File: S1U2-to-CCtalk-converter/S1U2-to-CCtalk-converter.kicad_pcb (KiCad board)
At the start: 2 copper layers, 136.2 x 73.1 mm, 23 parts, among them J1 DB9_Female, J2 CCtalk Cable, J3 CCtalk Cable, Q1 BC847, Q2 BC856, U1 ST232B, U2 L7805

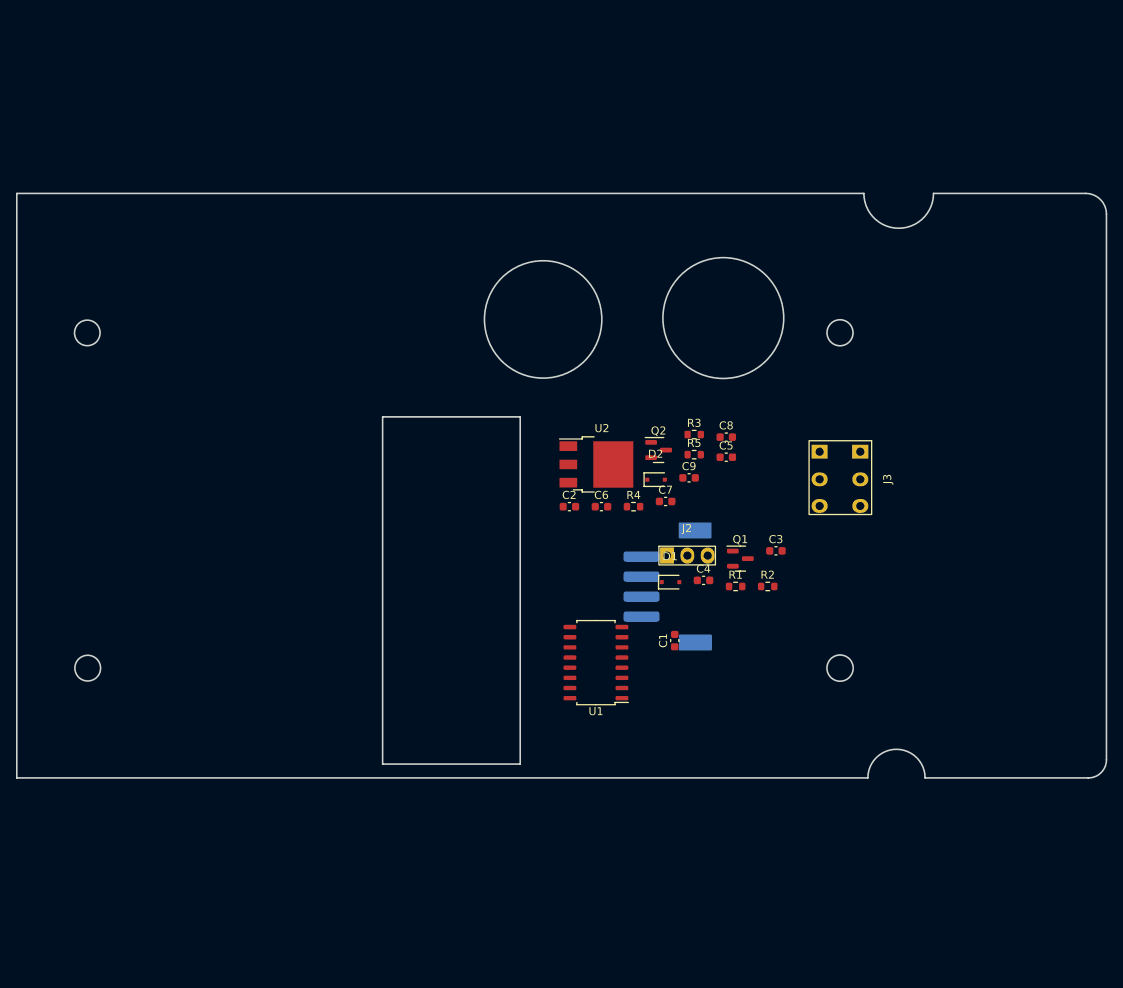
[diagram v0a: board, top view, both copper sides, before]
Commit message: add s1u2 dxf bckg and place components
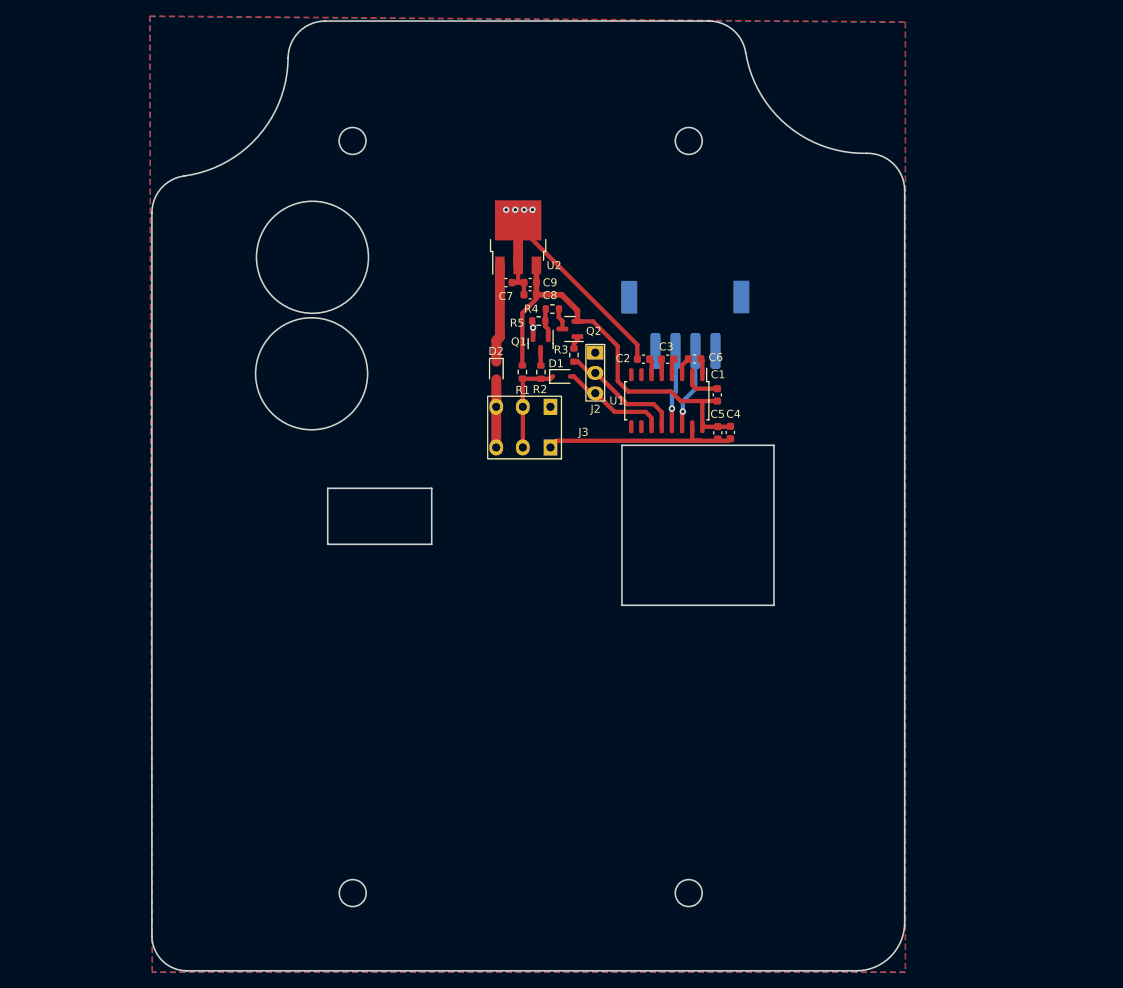
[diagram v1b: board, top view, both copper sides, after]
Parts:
- moved J3 39.7 mm to (140.3, 90.4), turned to 180 degrees
- moved R2 39.0 mm to (140.0, 80.9), turned to -90 degrees
- moved R1 37.8 mm to (137.7, 80.9), turned to -90 degrees
- moved Q1 36.7 mm to (140.0, 77.4), turned to -90 degrees
- moved J1 34.5 mm to (161.8, 78.3), turned to 180 degrees
- moved U1 33.9 mm to (155.7, 84.5), turned to -90 degrees
- moved C7 33.9 mm to (135.6, 69.8)
- moved C9 31.5 mm to (138.7, 69.8), turned to 180 degrees
- moved C1 31.2 mm to (162.0, 83.8)
- moved U2 30.9 mm to (137.2, 63.4), turned to 90 degrees
- moved C8 30.3 mm to (138.7, 71.3), turned to 180 degrees
- moved D1 29.1 mm to (142.6, 81.5)
- moved C3 27.5 mm to (155.8, 79.3), turned to 180 degrees
- moved J2 26.9 mm to (146.8, 78.5), turned to -90 degrees
- moved R4 26.7 mm to (141.4, 73.0), turned to 180 degrees
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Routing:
- net GNDREF: track 0.00 -> 62.9 mm, vias 0 -> 5
- net +5V: track 0.00 -> 51.4 mm
- net RX: track 0.00 -> 15.4 mm
- net TX: track 0.00 -> 13.3 mm
- net CCTALK-DATA: track 0.00 -> 12.5 mm
- net +24V: track 0.00 -> 12.2 mm
- net TXout: track 0.00 -> 10.3 mm, vias 0 -> 1
- net RXout: track 0.00 -> 8.64 mm, vias 0 -> 1
- net Net-(D2-Pad2): track 0.00 -> 8.53 mm
- net Net-(C1-Pad2): track 0.00 -> 4.60 mm
- net Net-(Q1-Pad1): track 0.00 -> 3.56 mm
- net Net-(Q2-Pad3): track 0.00 -> 2.71 mm
- net Net-(C6-Pad2): track 0.00 -> 2.30 mm
- net Net-(C6-Pad1): track 0.00 -> 2.06 mm
- net Net-(C3-Pad1): track 0.00 -> 2.04 mm
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- added copper zone on B.Cu, net GNDREF
- added copper zone on F.Cu, net GNDREF
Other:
- board size 136.2 x 73.1 mm -> 94.1 x 118.7 mm

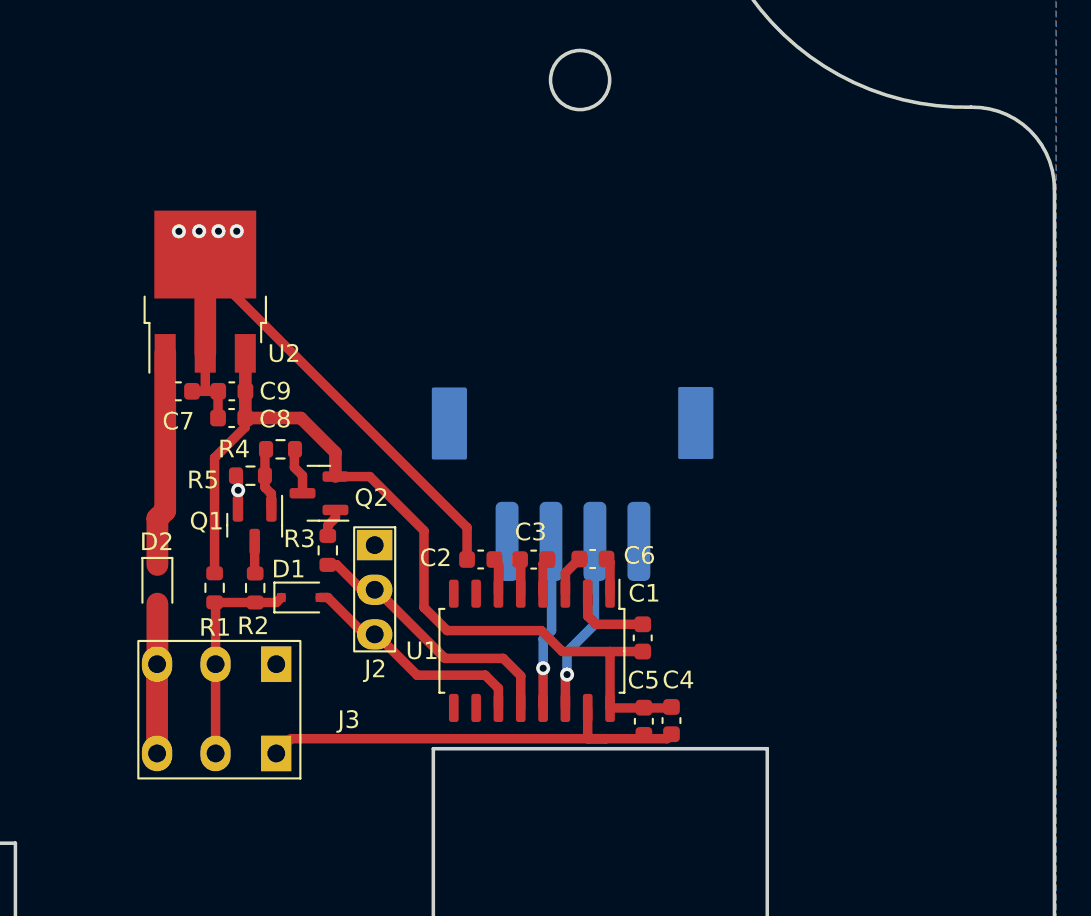
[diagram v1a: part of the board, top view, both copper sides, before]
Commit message: add paste silk screen
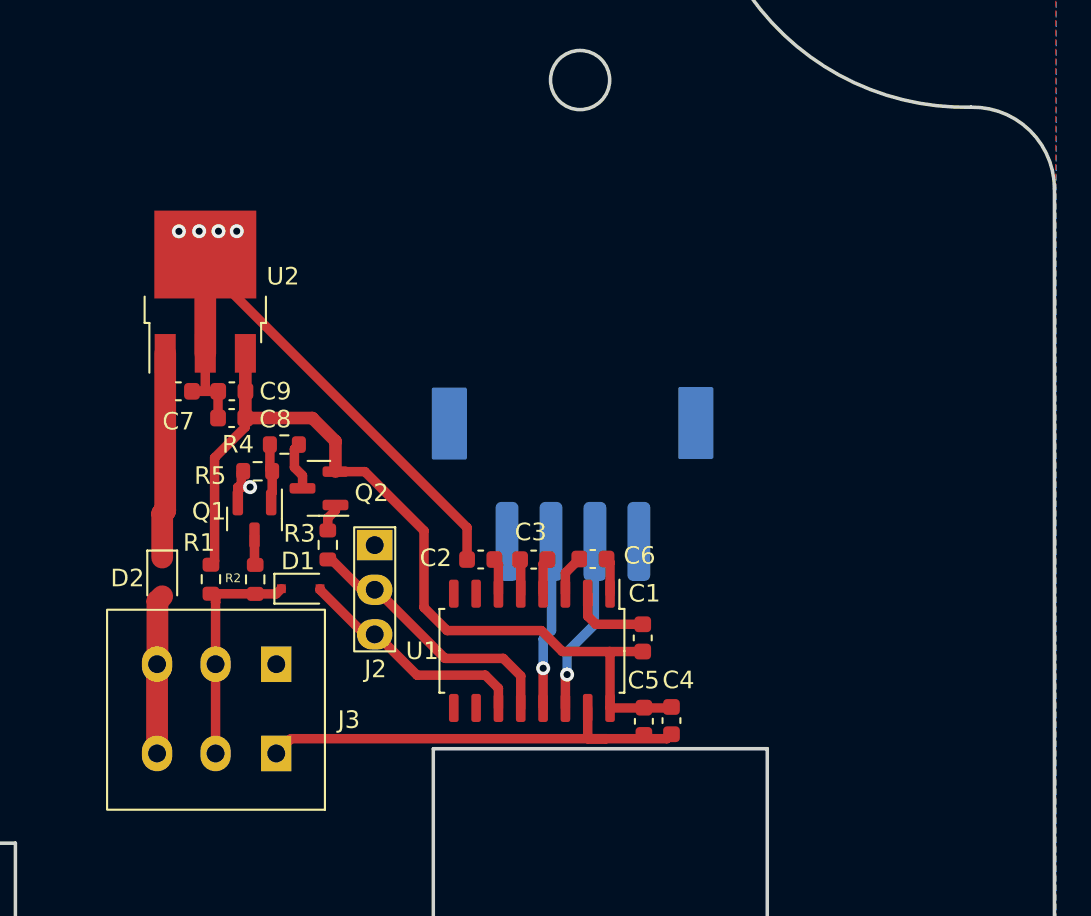
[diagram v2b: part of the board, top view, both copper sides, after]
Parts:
- moved R1 0.53 mm to (137.5, 80.4)
- moved D2 0.50 mm to (134.7, 80.3)
- moved D1 0.50 mm to (142.6, 81.0)
- moved R2 0.49 mm to (140.0, 80.5)
- moved R5 0.48 mm to (140.1, 74.3)
- moved Q1 0.36 mm to (139.9, 77.0)
- moved R4 0.35 mm to (141.7, 72.8)
- moved R3 0.31 mm to (144.1, 78.5)
- moved Q2 0.28 mm to (143.6, 75.3)
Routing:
- net CCTALK-DATA: track 12.5 -> 13.6 mm
- net GNDREF: track 62.9 -> 63.9 mm
- net Net-(D2-Pad2): track 8.53 -> 9.07 mm
- net +24V: track 12.2 -> 11.7 mm
